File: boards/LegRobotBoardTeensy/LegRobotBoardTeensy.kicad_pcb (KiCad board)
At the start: 2 copper layers, 169.2 x 91.1 mm, 116 parts, among them J1 IDC, J10 IDC, J11 IDC, J12 IDC, J13 IDC, J14 IDC, J15 IDC, J16 IDC, J2 B3B-XH-A, J3 B3B-XH-A, J4 B3B-XH-A, J5 B3B-XH-A, J6 IDC, J7 IDC, J8 IDC, J9 IDC, Q1 MMBT3904LT1G, Q10 MMBT3904LT1G, Q11 MMBT3904LT1G, Q12 MMBT3904LT1G, Q13 MMBT3904LT1G, Q14 MMBT3904LT1G, Q15 MMBT3904LT1G, Q16 MMBT3904LT1G, Q17 MMBT3904LT1G, Q18 MMBT3904LT1G, Q19 MMBT3904LT1G, Q2 MMBT3904LT1G, Q20 MMBT3904LT1G, Q21 MMBT3904LT1G, Q22 MMBT3904LT1G, Q23 MMBT3904LT1G, Q24 MMBT3904LT1G, Q3 MMBT3904LT1G, Q4 MMBT3904LT1G, Q5 MMBT3904LT1G, Q6 MMBT3904LT1G, Q7 MMBT3904LT1G, Q8 MMBT3904LT1G, Q9 MMBT3904LT1G, U1 Teensy4.0, U2 TLC555CDR, U3 SN74HC08DR, U4 SN74HC08DR, U5 PCA9685PW_118, U6 SN74HC08DR, U7 SN74HC08DR, U8 BNO055

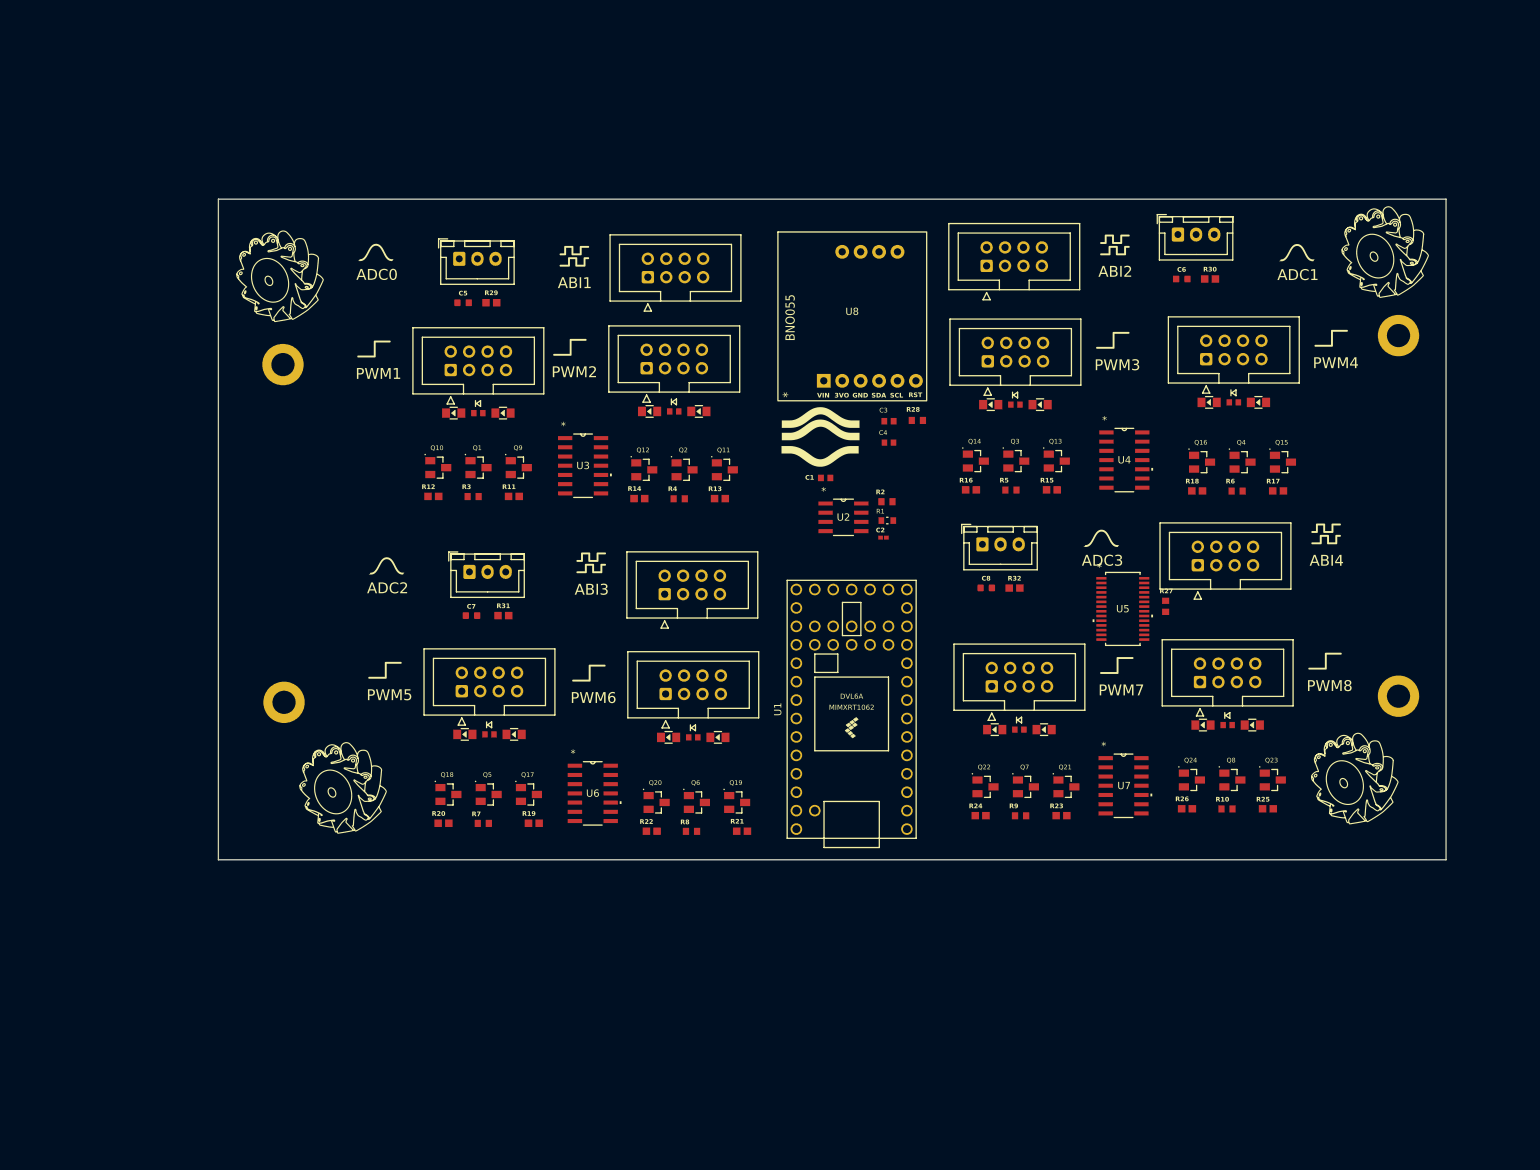
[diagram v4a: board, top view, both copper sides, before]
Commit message: Second iteration of leg robot board
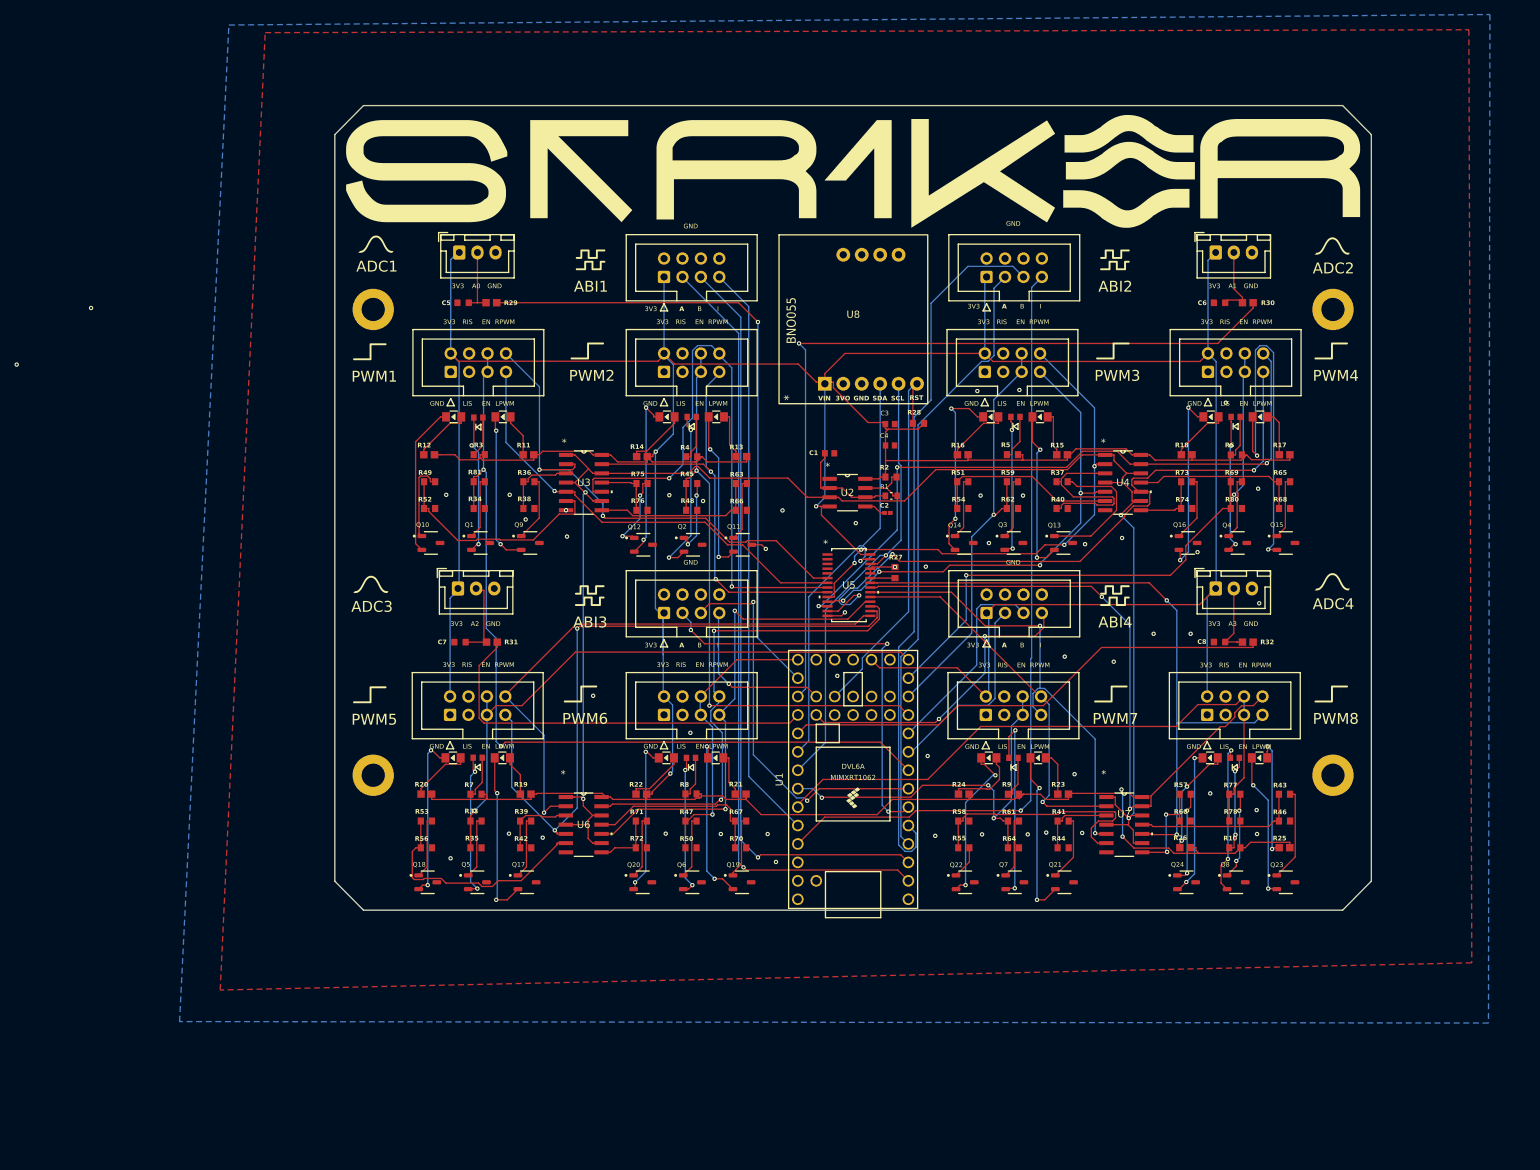
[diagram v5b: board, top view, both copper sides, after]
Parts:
- added R33: 10K, CRCW060310K0FKEA:CRCW060310K0FKEA, F.Cu at (72.1, 118.6)
- added R34: 100K, CRCW0603100KFKEA:CRCW0603100KFKEA, F.Cu at (72.5, 75.5)
- added R35: 100K, CRCW0603100KFKEA:CRCW0603100KFKEA, F.Cu at (72.1, 122.2)
- added R36: 10K, CRCW060310K0FKEA:CRCW060310K0FKEA, F.Cu at (79.3, 71.8)
- added R37: 10K, CRCW060310K0FKEA:CRCW060310K0FKEA, F.Cu at (152.8, 71.8)
- added R38: 100K, CRCW0603100KFKEA:CRCW0603100KFKEA, F.Cu at (79.3, 75.5)
- added R39: 10K, CRCW060310K0FKEA:CRCW060310K0FKEA, F.Cu at (78.9, 118.6)
- added R40: 100K, CRCW0603100KFKEA:CRCW0603100KFKEA, F.Cu at (152.8, 75.5)
- added R41: 10K, CRCW060310K0FKEA:CRCW060310K0FKEA, F.Cu at (153.0, 118.6)
- added R42: 100K, CRCW0603100KFKEA:CRCW0603100KFKEA, F.Cu at (78.9, 122.2)
- added R43: 10K, CRCW060310K0FKEA:CRCW060310K0FKEA, F.Cu at (183.5, 114.9)
- added R44: 100K, CRCW0603100KFKEA:CRCW0603100KFKEA, F.Cu at (153.0, 122.2)
- added R45: 10K, CRCW060310K0FKEA:CRCW060310K0FKEA, F.Cu at (101.8, 72.0)
- added R46: 100K, CRCW0603100KFKEA:CRCW0603100KFKEA, F.Cu at (183.5, 118.6)
- added R47: 10K, CRCW060310K0FKEA:CRCW060310K0FKEA, F.Cu at (101.7, 118.6)
- added R48: 100K, CRCW0603100KFKEA:CRCW0603100KFKEA, F.Cu at (101.8, 75.7)
- added R49: 10K, CRCW060310K0FKEA:CRCW060310K0FKEA, F.Cu at (65.7, 71.8)
- added R50: 100K, CRCW0603100KFKEA:CRCW0603100KFKEA, F.Cu at (101.7, 122.2)
- added R51: 10K, CRCW060310K0FKEA:CRCW060310K0FKEA, F.Cu at (139.1, 71.8)
- added R52: 100K, CRCW0603100KFKEA:CRCW0603100KFKEA, F.Cu at (65.7, 75.5)
- added R53: 10K, CRCW060310K0FKEA:CRCW060310K0FKEA, F.Cu at (65.2, 118.6)
- added R54: 100K, CRCW0603100KFKEA:CRCW0603100KFKEA, F.Cu at (139.1, 75.5)
- added R55: 10K, CRCW060310K0FKEA:CRCW060310K0FKEA, F.Cu at (139.3, 122.2)
- added R56: 100K, CRCW0603100KFKEA:CRCW0603100KFKEA, F.Cu at (65.2, 122.2)
- added R57: 10K, CRCW060310K0FKEA:CRCW060310K0FKEA, F.Cu at (169.8, 114.9)
- added R58: 100K, CRCW0603100KFKEA:CRCW0603100KFKEA, F.Cu at (139.3, 118.6)
- added R59: 10K, CRCW060310K0FKEA:CRCW060310K0FKEA, F.Cu at (146.0, 71.8)
- added R60: 100K, CRCW0603100KFKEA:CRCW0603100KFKEA, F.Cu at (169.8, 118.6)
- added R61: 10K, CRCW060310K0FKEA:CRCW060310K0FKEA, F.Cu at (146.1, 118.6)
- added R62: 100K, CRCW0603100KFKEA:CRCW0603100KFKEA, F.Cu at (146.0, 75.5)
- added R63: 10K, CRCW060310K0FKEA:CRCW060310K0FKEA, F.Cu at (108.6, 72.0)
- added R64: 100K, CRCW0603100KFKEA:CRCW0603100KFKEA, F.Cu at (146.1, 122.2)
- added R65: 10K, CRCW060310K0FKEA:CRCW060310K0FKEA, F.Cu at (183.5, 71.8)
- added R66: 100K, CRCW0603100KFKEA:CRCW0603100KFKEA, F.Cu at (108.6, 75.7)
- added R67: 10K, CRCW060310K0FKEA:CRCW060310K0FKEA, F.Cu at (108.5, 118.6)
- added R68: 100K, CRCW0603100KFKEA:CRCW0603100KFKEA, F.Cu at (183.5, 75.5)
- added R69: 10K, CRCW060310K0FKEA:CRCW060310K0FKEA, F.Cu at (176.8, 71.8)
- added R70: 100K, CRCW0603100KFKEA:CRCW0603100KFKEA, F.Cu at (108.5, 122.2)
- added R71: 10K, CRCW060310K0FKEA:CRCW060310K0FKEA, F.Cu at (94.8, 118.6)
- added R72: 100K, CRCW0603100KFKEA:CRCW0603100KFKEA, F.Cu at (94.8, 122.2)
- added R73: 10K, CRCW060310K0FKEA:CRCW060310K0FKEA, F.Cu at (170.0, 71.8)
- added R74: 100K, CRCW0603100KFKEA:CRCW0603100KFKEA, F.Cu at (170.0, 75.5)
- added R75: 10K, CRCW060310K0FKEA:CRCW060310K0FKEA, F.Cu at (94.9, 72.0)
- added R76: 100K, CRCW0603100KFKEA:CRCW0603100KFKEA, F.Cu at (94.9, 75.7)
- added R77: 10K, CRCW060310K0FKEA:CRCW060310K0FKEA, F.Cu at (176.6, 114.9)
- added R78: 100K, CRCW0603100KFKEA:CRCW0603100KFKEA, F.Cu at (176.6, 118.6)
- added R80: 100K, CRCW0603100KFKEA:CRCW0603100KFKEA, F.Cu at (176.8, 75.5)
- added R81: 10K, CRCW060310K0FKEA:CRCW060310K0FKEA, F.Cu at (72.5, 71.8)
- C2: value 0.01uF -> 10nF
- Q1, Q10, Q11, Q12, Q13, Q14, Q15, Q16, Q17, Q18, Q19, Q2, Q20, Q21, Q22, Q23, Q24, Q3, Q4, Q5, Q6, Q7, Q8, Q9: value MMBT3904LT1G -> AO3400A; footprint SMMBT3904LT1G:MMBT3904LT1G -> AO3400A:AO3400A
- moved U5 37.9 mm to (123.5, 86.0)
- moved R27 37.6 mm to (129.8, 84.3)
- moved C8 33.0 mm to (174.5, 93.9)
- moved R32 33.0 mm to (178.4, 93.9)
- moved J5 32.7 mm to (174.0, 86.5)
- moved J16 29.8 mm to (142.4, 89.9)
- moved MH3 15.9 mm to (57.9, 112.2)
- moved MH1 14.6 mm to (57.9, 48.0)
- moved Q23 14.2 mm to (183.7, 127.0)
- moved MH4 14.2 mm to (190.2, 112.2)
- moved Q24 14.1 mm to (170.0, 127.0)
- moved Q8 14.1 mm to (176.8, 127.0)
- moved Q22 13.4 mm to (139.5, 127.0)
- moved Q7 13.2 mm to (146.3, 127.0)
- moved Q21 13.2 mm to (153.2, 127.0)
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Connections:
- Q1 pad 1: PWMEN1 -> Net-(Q1-Pad1)
- Q1 pad 2: GND -> Net-(D1-K)
- Q1 pad 3: Net-(D1-K) -> GND
- Q10 pad 1: LPWM1BLINK -> Net-(Q10-Pad1)
- Q10 pad 2: GND -> Net-(D10-K)
- Q10 pad 3: Net-(D10-K) -> GND
- Q11 pad 1: RPWM2BLINK -> Net-(Q11-Pad1)
- Q11 pad 2: GND -> Net-(D11-K)
- Q11 pad 3: Net-(D11-K) -> GND
- Q12 pad 1: LPWM2BLINK -> Net-(Q12-Pad1)
- Q12 pad 2: GND -> Net-(D12-K)
- Q12 pad 3: Net-(D12-K) -> GND
- Q13 pad 1: RPWM3BLINK -> Net-(Q13-Pad1)
- Q13 pad 2: GND -> Net-(D13-K)
- Q13 pad 3: Net-(D13-K) -> GND
- Q14 pad 1: LPWM3BLINK -> Net-(Q14-Pad1)
- Q14 pad 2: GND -> Net-(D14-K)
- Q14 pad 3: Net-(D14-K) -> GND
- Q15 pad 1: RPWM4BLINK -> Net-(Q15-Pad1)
- Q15 pad 2: GND -> Net-(D15-K)
- Q15 pad 3: Net-(D15-K) -> GND
- Q16 pad 1: LPWM4BLINK -> Net-(Q16-Pad1)
- Q16 pad 2: GND -> Net-(D16-K)
- Q16 pad 3: Net-(D16-K) -> GND
- Q17 pad 1: RPWM5BLINK -> Net-(Q17-Pad1)
- Q17 pad 2: GND -> Net-(D17-K)
- Q17 pad 3: Net-(D17-K) -> GND
- Q18 pad 1: LPWM5BLINK -> Net-(Q18-Pad1)
- Q18 pad 2: GND -> Net-(D18-K)
- Q18 pad 3: Net-(D18-K) -> GND
- Q19 pad 1: RPWM6BLINK -> Net-(Q19-Pad1)
- Q19 pad 2: GND -> Net-(D19-K)
- Q19 pad 3: Net-(D19-K) -> GND
- Q2 pad 1: PWMEN2 -> Net-(Q2-Pad1)
- Q2 pad 2: GND -> Net-(D2-K)
- Q2 pad 3: Net-(D2-K) -> GND
- Q20 pad 1: LPWM6BLINK -> Net-(Q20-Pad1)
- Q20 pad 2: GND -> Net-(D20-K)
- Q20 pad 3: Net-(D20-K) -> GND
- Q21 pad 1: RPWM7BLINK -> Net-(Q21-Pad1)
- Q21 pad 2: GND -> Net-(D21-K)
- Q21 pad 3: Net-(D21-K) -> GND
- Q22 pad 1: LPWM7BLINK -> Net-(Q22-Pad1)
- Q22 pad 2: GND -> Net-(D22-K)
- Q22 pad 3: Net-(D22-K) -> GND
- Q23 pad 1: RPWM8BLINK -> Net-(Q23-Pad1)
- Q23 pad 2: GND -> Net-(D23-K)
- Q23 pad 3: Net-(D23-K) -> GND
- Q24 pad 1: LPWM8BLINK -> Net-(Q24-Pad1)
- Q24 pad 2: GND -> Net-(D24-K)
- Q24 pad 3: Net-(D24-K) -> GND
- Q3 pad 1: PWMEN3 -> Net-(Q3-Pad1)
- Q3 pad 2: GND -> Net-(D3-K)
- Q3 pad 3: Net-(D3-K) -> GND
- Q4 pad 1: PWMEN4 -> Net-(Q4-Pad1)
- Q4 pad 2: GND -> Net-(D4-K)
- Q4 pad 3: Net-(D4-K) -> GND
- Q5 pad 1: PWMEN5 -> Net-(Q5-Pad1)
- Q5 pad 2: GND -> Net-(D5-K)
- Q5 pad 3: Net-(D5-K) -> GND
- Q6 pad 1: PWMEN6 -> Net-(Q6-Pad1)
- Q6 pad 2: GND -> Net-(D6-K)
- Q6 pad 3: Net-(D6-K) -> GND
- Q7 pad 1: PWMEN7 -> Net-(Q7-Pad1)
- Q7 pad 2: GND -> Net-(D7-K)
- Q7 pad 3: Net-(D7-K) -> GND
- Q8 pad 1: PWMEN8 -> Net-(Q8-Pad1)
- Q8 pad 2: GND -> Net-(D8-K)
- Q8 pad 3: Net-(D8-K) -> GND
- Q9 pad 1: RPWM1BLINK -> Net-(Q9-Pad1)
- Q9 pad 2: GND -> Net-(D9-K)
- Q9 pad 3: Net-(D9-K) -> GND
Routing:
- net +3.3V: track 0.00 -> 704.4 mm, vias 0 -> 5
- net BLINK: track 0.00 -> 221.7 mm, vias 0 -> 4
- net PWMEN1: track 0.00 -> 119.5 mm, vias 0 -> 2
- net A1: track 0.00 -> 114.8 mm, vias 0 -> 1
- net ENCODER1_A: track 0.00 -> 108.3 mm, vias 0 -> 1
- net ENCODER2_I: track 0.00 -> 107.4 mm, vias 0 -> 1
- net ENCODER1_B: track 0.00 -> 104.5 mm, vias 0 -> 1
- net ENCODER2_B: track 0.00 -> 98.4 mm
- net LPWM4: track 0.00 -> 95.0 mm, vias 0 -> 3
- net RPWM4: track 0.00 -> 93.5 mm, vias 0 -> 3
- net LPWM5: track 0.00 -> 93.5 mm, vias 0 -> 2
- net LPWM8: track 0.00 -> 91.8 mm, vias 0 -> 2
- net RPWM8: track 0.00 -> 89.3 mm, vias 0 -> 2
- net A0: track 0.00 -> 88.5 mm, vias 0 -> 1
- net PWMEN8: track 0.00 -> 86.4 mm
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- added copper zone on B.Cu, net GND
- added copper zone on F.Cu, net GND
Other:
- board size 169.2 x 91.1 mm -> 142.8 x 110.9 mm
- board text added: "3V3"
- board text added: "A"
- board text added: "A0"
- board text added: "A1"
- board text added: "A2"
- board text added: "A3"
- board text added: "ADC4"
- board text added: "B"
- board text added: "EN"
- board text added: "GND"
- board text added: "I"
- board text added: "LIS"
- board text added: "LPWM"
- board text added: "RIS"
- board text added: "RPWM"
- board text removed: "ADC0"
